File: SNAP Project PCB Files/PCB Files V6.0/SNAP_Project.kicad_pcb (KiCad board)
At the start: 4 copper layers, 66.7 x 47.2 mm, 108 parts, among them IC1 ADP121-AUJZ30R7, IC2 STM32WB35CCU7A, J1 USB_C_Receptacle_USB2.0, J3 Serial Wire Debug, J4 OLED Screen Conn, Q1 2N7000, Q2 2N7000, Q3 2N7000, Q4 SFH 310, Q5 2N7002KDW_R1_00001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

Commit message: Fix Button Issue
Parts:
- removed R29: 10k, Resistor_SMD:R_0805_2012Metric
- turned C30 to 0 degrees
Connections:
- SW5 pad 1: BUTT_2 -> GND
- SW5 pad 2: +3V0 -> BUTT_2
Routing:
- net GND: track 99.2 -> 90.2 mm, vias 344 -> 345
- net BUTT_2: track 0.86 -> 9.88 mm, vias 1 -> 0
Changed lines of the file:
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@@
   )
   (footprint "Capacitor_SMD:C_0402_1005Metric" (layer "F.Cu")
-    (at 106.37 89.8075 180)
+    (at 106.37 89.8075)
     (descr "Capacitor SMD 0402 (1005 Metric), square (rectangular) end terminal, IPC_7351 nominal, (Body size source: IPC-SM-782 page 76, https://www.pcb-3d.com/wordpress/wp-content/uploads/ipc-sm-782a_amendment_1_and_2.pdf), generated with kicad-footprint-generator")
     (tags "capacitor")
@@
     (fp_line (start 0.5 -0.25) (end 0.5 0.25) (layer "F.Fab") (width 0.1))
     (fp_line (start 0.5 0.25) (end -0.5 0.25) (layer "F.Fab") (width 0.1))
-    (pad "1" smd roundrect (at -0.48 0 180) (size 0.56 0.62) (layers "F.Cu" "F.Paste" "F.Mask") (roundrect_rratio 0.25)
+    (pad "1" smd roundrect (at -0.48 0) (size 0.56 0.62) (layers "F.Cu" "F.Paste" "F.Mask") (roundrect_rratio 0.25)
       (net 2 "GND") (pintype "passive"))
-    (pad "2" smd roundrect (at 0.48 0 180) (size 0.56 0.62) (layers "F.Cu" "F.Paste" "F.Mask") (roundrect_rratio 0.25)
+    (pad "2" smd roundrect (at 0.48 0) (size 0.56 0.62) (layers "F.Cu" "F.Paste" "F.Mask") (roundrect_rratio 0.25)
       (net 26 "BUTT_2") (pintype "passive"))
     (model "${KICAD6_3DMODEL_DIR}/Capacitor_SMD.3dshapes/C_0402_1005Metric.wrl"
@@
       (net 2 "GND") (pintype "passive"))
     (model "${KICAD6_3DMODEL_DIR}/Capacitor_SMD.3dshapes/C_0402_1005Metric.wrl"
-      (offset (xyz 0 0 0))
-      (scale (xyz 1 1 1))
-      (rotate (xyz 0 0 0))
-    )
-  )
-  (footprint "Resistor_SMD:R_0805_2012Metric" (layer "F.Cu")
-    (at 104.24 72.17)
-    (descr "Resistor SMD 0805 (2012 Metric), square (rectangular) end terminal, IPC_7351 nominal, (Body size source: IPC-SM-782 page 72, https://www.pcb-3d.com/wordpress/wp-content/uploads/ipc-sm-782a_amendment_1_and_2.pdf), generated with kicad-footprint-generator")
-    (tags "resistor")
-    (property "Sheetfile" "RF_MPU_OPAMP_PH.kicad_sch")
-    (property "Sheetname" "Amplification + Phototransistor + RF + MPU Circuit")
-    (attr smd)
-    (fp_text reference "R29" (at 0 -1.65) (layer "F.SilkS")
-      (effects (font (size 1 1) (thickness 0.15)))
-    )
-    (fp_text value "10k" (at 0 1.65) (layer "F.Fab")
-      (effects (font (size 1 1) (thickness 0.15)))
-    )
-    (fp_text user "${REFERENCE}" (at 0 0) (layer "F.Fab")
-      (effects (font (size 0.5 0.5) (thickness 0.08)))
-    )
-    (fp_line (start -0.227064 0.735) (end 0.227064 0.735) (layer "F.SilkS") (width 0.12))
-    (fp_line (start -0.227064 -0.735) (end 0.227064 -0.735) (layer "F.SilkS") (width 0.12))
-    (fp_line (start 1.68 -0.95) (end 1.68 0.95) (layer "F.CrtYd") (width 0.05))
-    (fp_line (start 1.68 0.95) (end -1.68 0.95) (layer "F.CrtYd") (width 0.05))
-    (fp_line (start -1.68 -0.95) (end 1.68 -0.95) (layer "F.CrtYd") (width 0.05))
-    (fp_line (start -1.68 0.95) (end -1.68 -0.95) (layer "F.CrtYd") (width 0.05))
-    (fp_line (start 1 0.625) (end -1 0.625) (layer "F.Fab") (width 0.1))
-    (fp_line (start -1 -0.625) (end 1 -0.625) (layer "F.Fab") (width 0.1))
-    (fp_line (start 1 -0.625) (end 1 0.625) (layer "F.Fab") (width 0.1))
-    (fp_line (start -1 0.625) (end -1 -0.625) (layer "F.Fab") (width 0.1))
-    (pad "1" smd roundrect (at -0.9125 0) (size 1.025 1.4) (layers "F.Cu" "F.Paste" "F.Mask") (roundrect_rratio 0.243902)
-      (net 26 "BUTT_2") (pintype "passive"))
-    (pad "2" smd roundrect (at 0.9125 0) (size 1.025 1.4) (layers "F.Cu" "F.Paste" "F.Mask") (roundrect_rratio 0.243902)
-      (net 2 "GND") (pintype "passive"))
-    (model "${KICAD6_3DMODEL_DIR}/Resistor_SMD.3dshapes/R_0805_2012Metric.wrl"
       (offset (xyz 0 0 0))
       (scale (xyz 1 1 1))
@@
     (fp_line (start -1.27 -2.92) (end -1.27 2.88) (layer "F.Fab") (width 0.1))
     (pad "1" thru_hole roundrect (at 0 0) (size 1.74 2.19) (drill 1.19) (layers *.Cu *.Mask) (roundrect_rratio 0.1436781609)
-      (net 26 "BUTT_2") (pinfunction "1") (pintype "passive"))
+      (net 2 "GND") (pinfunction "1") (pintype "passive"))
     (pad "2" thru_hole oval (at 2.54 0) (size 1.74 2.19) (drill 1.19) (layers *.Cu *.Mask)
-      (net 3 "+3V0") (pinfunction "2") (pintype "passive"))
+      (net 26 "BUTT_2") (pinfunction "2") (pintype "passive"))
     (model "${KICAD6_3DMODEL_DIR}/Connector_Molex.3dshapes/Molex_KK-254_AE-6410-02A_1x02_P2.54mm_Vertical.wrl"
       (offset (xyz 0 0 0))
@@
   (segment (start 113.88 95.12) (end 114.4 95.12) (width 0.25) (layer "F.Cu") (net 2))
   (segment (start 109.35 96.8075) (end 107.6 98.5575) (width 0.25) (layer "F.Cu") (net 2))
-  (segment (start 107.85 91.55) (end 107.85 95.1075) (width 0.25) (layer "F.Cu") (net 2))
   (segment (start 103.13 102.75) (end 103.44 103.06) (width 0.25) (layer "F.Cu") (net 2))
   (segment (start 99.125 111.075) (end 99.365773 111.315773) (width 0.25) (layer "F.Cu") (net 2))
@@
   (segment (start 75.94 109.7725) (end 75.34 110.3725) (width 1) (layer "F.Cu") (net 2))
   (segment (start 127.805 86.5425) (end 127.805 85.6175) (width 0.25) (layer "F.Cu") (net 2))
-  (segment (start 107.54 87.3675) (end 106.85 88.0575) (width 0.25) (layer "F.Cu") (net 2))
   (segment (start 118.3625 113.2975) (end 118.9975 113.2975) (width 0.5) (layer "F.Cu") (net 2))
   (segment (start 103.44 103.06) (end 103.44 102.54) (width 0.25) (layer "F.Cu") (net 2))
@@
   (segment (start 111.2 94.92) (end 111.2 94.58) (width 0.25) (layer "F.Cu") (net 2))
   (segment (start 106.47 107.28) (end 106.47 106.8575) (width 0.25) (layer "F.Cu") (net 2))
-  (segment (start 106.85 88.0575) (end 106.85 89.8075) (width 0.25) (layer "F.Cu") (net 2))
   (segment (start 103.2 103.3) (end 103.44 103.06) (width 0.25) (layer "F.Cu") (net 2))
   (segment (start 109.58 105.4875) (end 109.58 106.13) (width 0.25) (layer "F.Cu") (net 2))
@@
   (segment (start 119.83 113.3) (end 120.45 113.92) (width 0.5) (layer "F.Cu") (net 2))
   (segment (start 114.3175 92.8275) (end 114.325 92.82) (width 0.25) (layer "F.Cu") (net 2))
-  (segment (start 106.85 90.55) (end 107.85 91.55) (width 0.25) (layer "F.Cu") (net 2))
   (segment (start 111.525 118.145) (end 111.71 117.96) (width 0.25) (layer "F.Cu") (net 2))
   (segment (start 118.98 107.855) (end 118.98 108.355) (width 0.25) (layer "F.Cu") (net 2))
+  (segment (start 105.89 89.8075) (end 105.89 88.96) (width 0.25) (layer "F.Cu") (net 2))
   (segment (start 111.525 119.1) (end 111.525 118.145) (width 0.25) (layer "F.Cu") (net 2))
   (segment (start 88.875 108.4075) (end 88.875 110.25) (width 0.6) (layer "F.Cu") (net 2))
@@
   (segment (start 115.069273 116.125) (end 115.076773 116.1175) (width 0.25) (layer "F.Cu") (net 2))
   (segment (start 100.47 97.1075) (end 99.7875 97.1075) (width 0.25) (layer "F.Cu") (net 2))
-  (segment (start 106.85 89.8075) (end 106.85 90.55) (width 0.25) (layer "F.Cu") (net 2))
   (segment (start 113.875 116.125) (end 115.069273 116.125) (width 0.25) (layer "F.Cu") (net 2))
   (segment (start 86.65 92.425) (end 86.65 92.25) (width 0.25) (layer "F.Cu") (net 2))
@@
   (segment (start 110.625 112.35) (end 110.65 112.375) (width 0.25) (layer "F.Cu") (net 2))
   (segment (start 115.91 98.81) (end 115.925 98.825) (width 0.25) (layer "F.Cu") (net 2))
-  (segment (start 107.54 85.9275) (end 107.54 87.3675) (width 0.25) (layer "F.Cu") (net 2))
   (segment (start 105.35 92.5275) (end 105.35 91.675) (width 0.25) (layer "F.Cu") (net 2))
   (segment (start 128.0775 85.29) (end 128.055 85.2675) (width 0.25) (layer "F.Cu") (net 2))
   (segment (start 127.805 85.6175) (end 128.055 85.3675) (width 0.25) (layer "F.Cu") (net 2))
+  (segment (start 105.89 88.96) (end 105.9 88.95) (width 0.25) (layer "F.Cu") (net 2))
   (segment (start 94.75 97.8) (end 94.75 98.5775) (width 0.25) (layer "F.Cu") (net 2))
   (via (at 86.325 78.95) (size 0.55) (drill 0.25) (layers "F.Cu" "B.Cu") (net 2))
@@
   (via (at 123.26 115.93) (size 0.55) (drill 0.25) (layers "F.Cu" "B.Cu") (net 2))
   (via (at 101.25 120.52) (size 0.55) (drill 0.25) (layers "F.Cu" "B.Cu") (net 2))
+  (via (at 105.9 88.95) (size 0.55) (drill 0.25) (layers "F.Cu" "B.Cu") (net 2))
   (via (at 132.8 92.375) (size 0.55) (drill 0.25) (layers "F.Cu" "B.Cu") (net 2))
   (via (at 86.53 111.36) (size 0.55) (drill 0.25) (layers "F.Cu" "B.Cu") (net 2))
@@
   (segment (start 113.08 90.3775) (end 112.95 90.5075) (width 0.25) (layer "F.Cu") (net 25))
   (segment (start 113.84 85.9275) (end 113.84 87.9175) (width 0.25) (layer "F.Cu") (net 25))
-  (segment (start 105.89 89.8075) (end 105.89 88.96) (width 0.25) (layer "F.Cu") (net 26))
-  (segment (start 105.89 88.96) (end 105.9 88.95) (width 0.25) (layer "F.Cu") (net 26))
-  (via (at 105.9 88.95) (size 0.55) (drill 0.25) (layers "F.Cu" "B.Cu") (net 26))
+  (segment (start 107.85 91.55) (end 107.85 95.1075) (width 0.25) (layer "F.Cu") (net 26))
+  (segment (start 107.54 87.3675) (end 106.85 88.0575) (width 0.25) (layer "F.Cu") (net 26))
+  (segment (start 106.85 88.0575) (end 106.85 89.8075) (width 0.25) (layer "F.Cu") (net 26))
+  (segment (start 106.85 90.55) (end 107.85 91.55) (width 0.25) (layer "F.Cu") (net 26))
+  (segment (start 106.85 89.8075) (end 106.85 90.55) (width 0.25) (layer "F.Cu") (net 26))
+  (segment (start 107.54 85.9275) (end 107.54 87.3675) (width 0.25) (layer "F.Cu") (net 26))
   (segment (start 112 101.17) (end 112 101.770293) (width 0.2) (layer "F.Cu") (net 27))
   (segment (start 111.05 100.8075) (end 111.6375 100.8075) (width 0.2) (layer "F.Cu") (net 27))

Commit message: 4v Line fix
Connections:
- C2 pad 1: +3V0 -> +4V
- C3 pad 1: SW_ON -> +4V
- IC1 pad 5: +3V0 -> +4V
- L1 pad 1: SW_ON -> +4V
- U2 pad 5: SW_ON -> +4V
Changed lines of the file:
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@@
   (net 89 "Net-(C25-Pad1)")
   (net 90 "Net-(R18-Pad2)")
+  (net 91 "+4V")
   (footprint "Connector_Molex:Molex_KK-254_AE-6410-04A_1x04_P2.54mm_Vertical" (layer "F.Cu")
     (at 95.14 78.9275)
@@
       (net 20 "unconnected-(IC1-Pad4)") (pinfunction "NC") (pintype "no_connect"))
     (pad "5" smd rect locked (at 1.25 -0.95 180) (size 0.6 1.15) (layers "F.Cu" "F.Paste" "F.Mask")
-      (net 3 "+3V0") (pinfunction "VOUT") (pintype "passive"))
+      (net 91 "+4V") (pinfunction "VOUT") (pintype "passive"))
     (model "F:\\KiCad Libraries\\SamacSys_Parts.3dshapes\\ADP121-AUJZ33R7.stp"
       (offset (xyz 0 0 0))
@@
       (net 28 "MT3608_EN") (pinfunction "EN") (pintype "input"))
     (pad "5" smd roundrect (at 1.1375 0 270) (size 1.325 0.6) (layers "F.Cu" "F.Paste" "F.Mask") (roundrect_rratio 0.25)
-      (net 1 "SW_ON") (pinfunction "IN") (pintype "power_in"))
+      (net 91 "+4V") (pinfunction "IN") (pintype "power_in"))
     (pad "6" smd roundrect (at 1.1375 -0.95 270) (size 1.325 0.6) (layers "F.Cu" "F.Paste" "F.Mask") (roundrect_rratio 0.25)
       (net 67 "unconnected-(U2-Pad6)") (pinfunction "NC") (pintype "no_connect"))
@@
     (fp_line (start 1.6 -0.8) (end 1.6 0.8) (layer "F.Fab") (width 0.1))
     (pad "1" smd roundrect (at -1.475 0 180) (size 1.15 1.8) (layers "F.Cu" "F.Paste" "F.Mask") (roundrect_rratio 0.2173913043)
-      (net 3 "+3V0") (pintype "passive"))
+      (net 91 "+4V") (pintype "passive"))
     (pad "2" smd roundrect (at 1.475 0 180) (size 1.15 1.8) (layers "F.Cu" "F.Paste" "F.Mask") (roundrect_rratio 0.2173913043)
       (net 2 "GND") (pintype "passive"))
@@
     (fp_line (start 1.6 -0.8) (end 1.6 0.8) (layer "F.Fab") (width 0.1))
     (pad "1" smd roundrect (at -1.475 0 180) (size 1.15 1.8) (layers "F.Cu" "F.Paste" "F.Mask") (roundrect_rratio 0.2173913043)
-      (net 1 "SW_ON") (pintype "passive"))
+      (net 91 "+4V") (pintype "passive"))
     (pad "2" smd roundrect (at 1.475 0 180) (size 1.15 1.8) (layers "F.Cu" "F.Paste" "F.Mask") (roundrect_rratio 0.2173913043)
       (net 2 "GND") (pintype "passive"))
@@
     (fp_line (start -2.54 2.54) (end 2.54 2.54) (layer "F.Fab") (width 0.1))
     (pad "1" smd rect (at -2.4265 0) (size 1.903 2.79) (layers "F.Cu" "F.Paste" "F.Mask")
-      (net 1 "SW_ON") (pintype "passive"))
+      (net 91 "+4V") (pintype "passive"))
     (pad "2" smd rect (at 2.4265 0) (size 1.903 2.79) (layers "F.Cu" "F.Paste" "F.Mask")
       (net 15 "Net-(D1-Pad2)") (pintype "passive"))

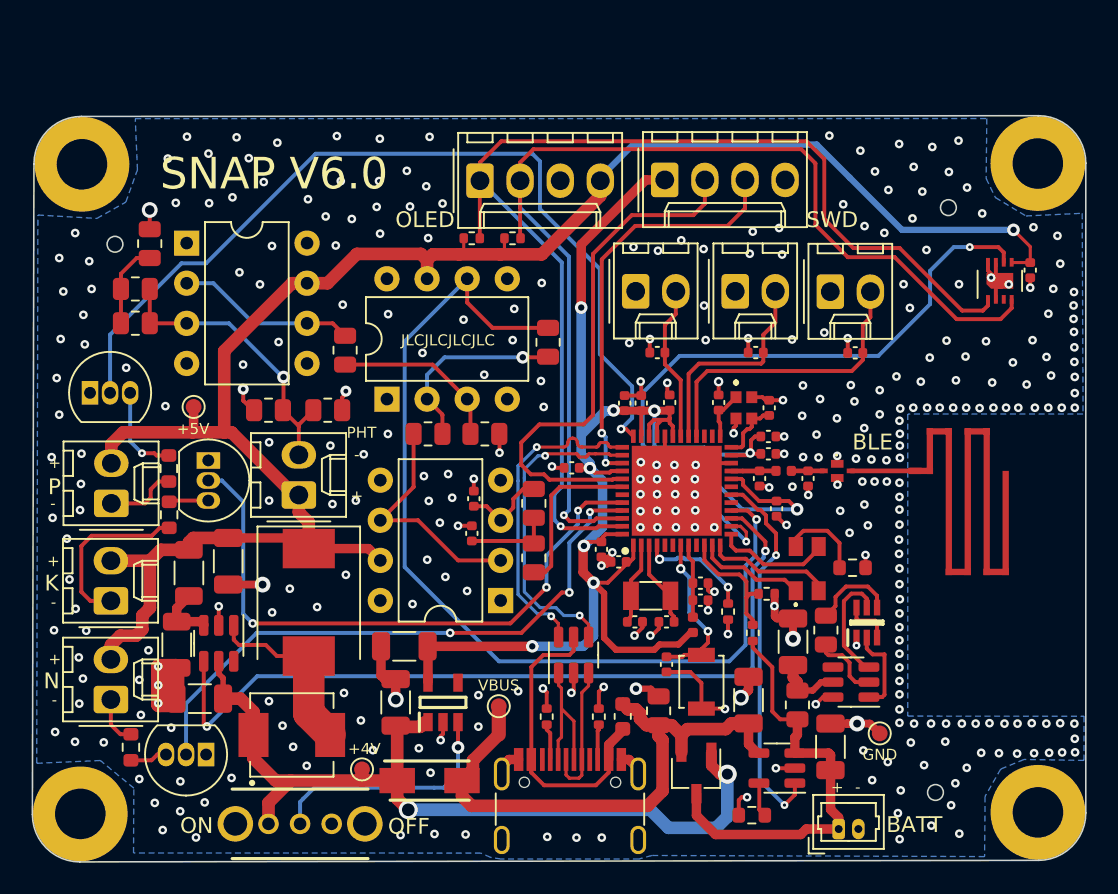
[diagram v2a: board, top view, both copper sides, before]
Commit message: USB Parity Fix
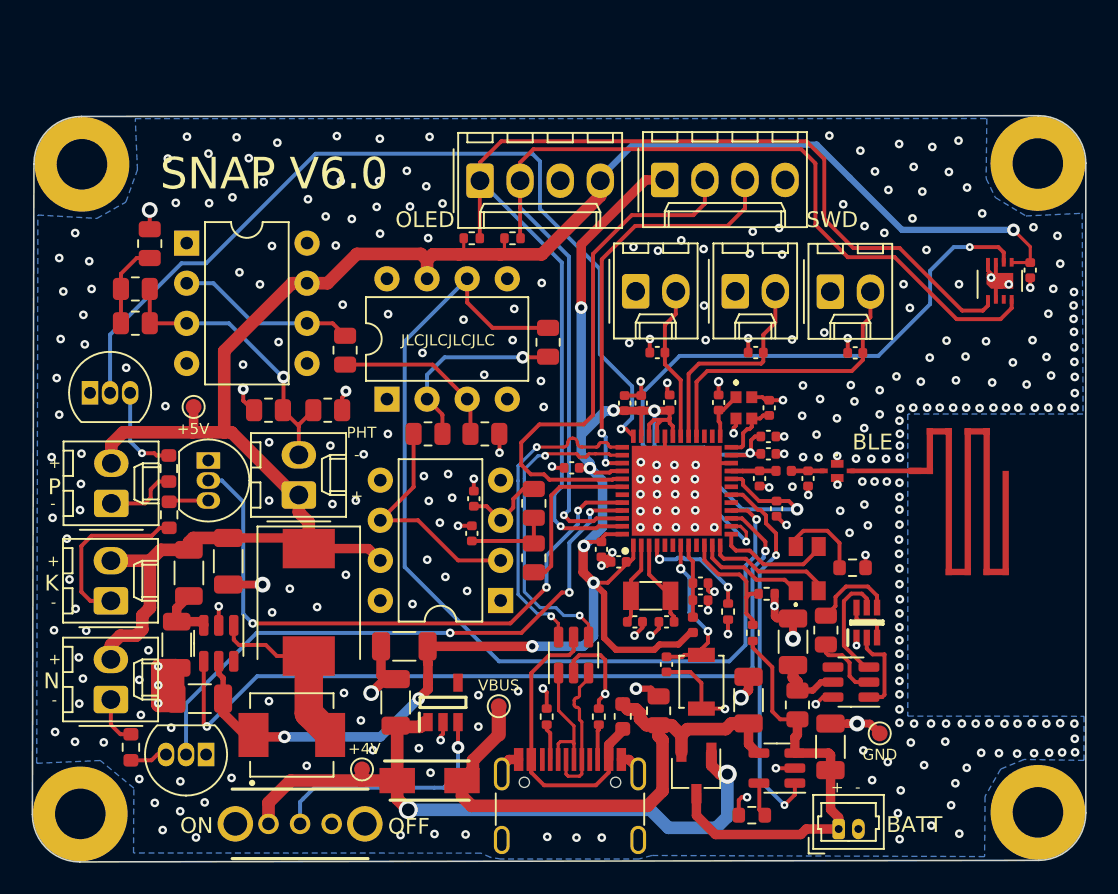
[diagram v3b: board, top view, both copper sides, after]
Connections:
- C2 pad 1: +4V -> +3V0
- C3 pad 1: +4V -> +3V0
- IC1 pad 5: +4V -> +3V0
- L1 pad 1: +4V -> +3V0
- U2 pad 5: +4V -> +3V0
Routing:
- net +3V0: track 104.3 -> 122.9 mm, vias 9 -> 11
- net SW_ON: track 55.0 -> 44.4 mm
- net GND: track 90.2 -> 94.3 mm, vias 345 -> 342
- net USB_CONN_D-: track 9.18 -> 7.98 mm
- added copper zone on In2.Cu, net GND
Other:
- outline, holes or cut-outs redrawn

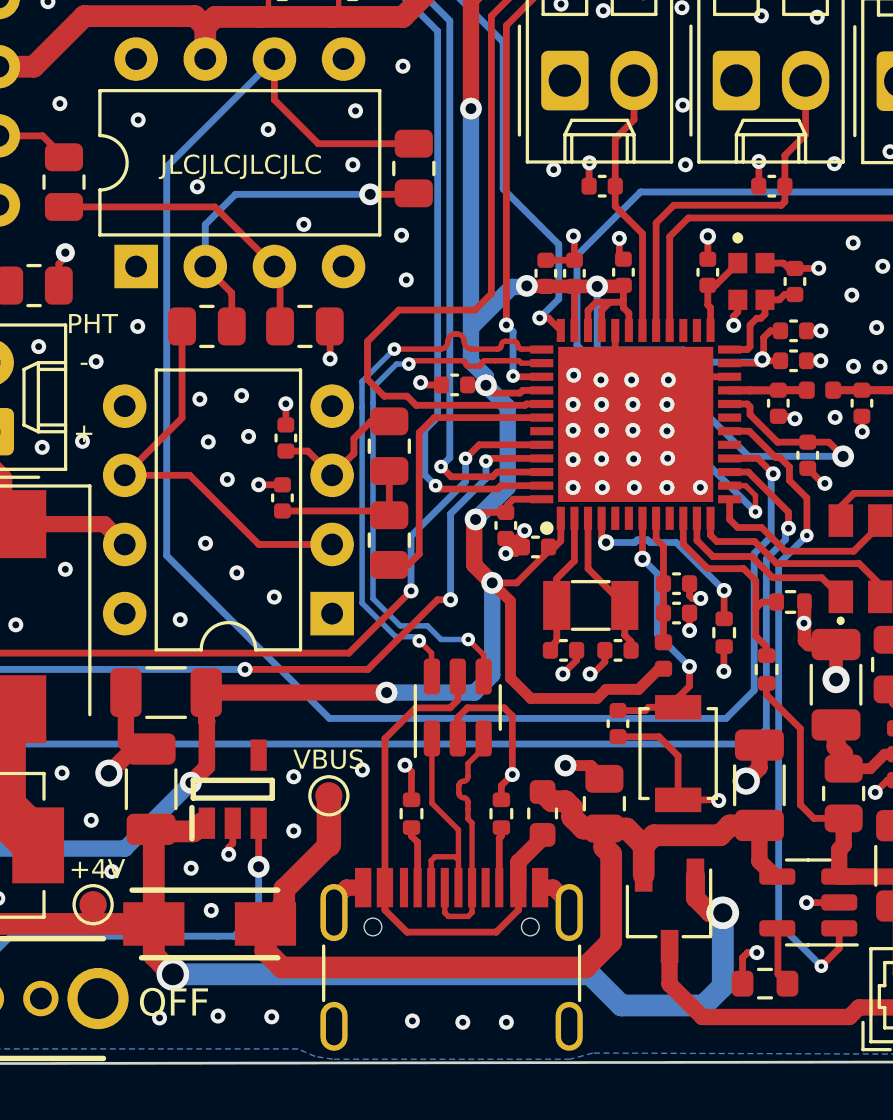
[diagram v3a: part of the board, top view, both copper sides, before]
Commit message: USB Fix 2 & 3V line fix
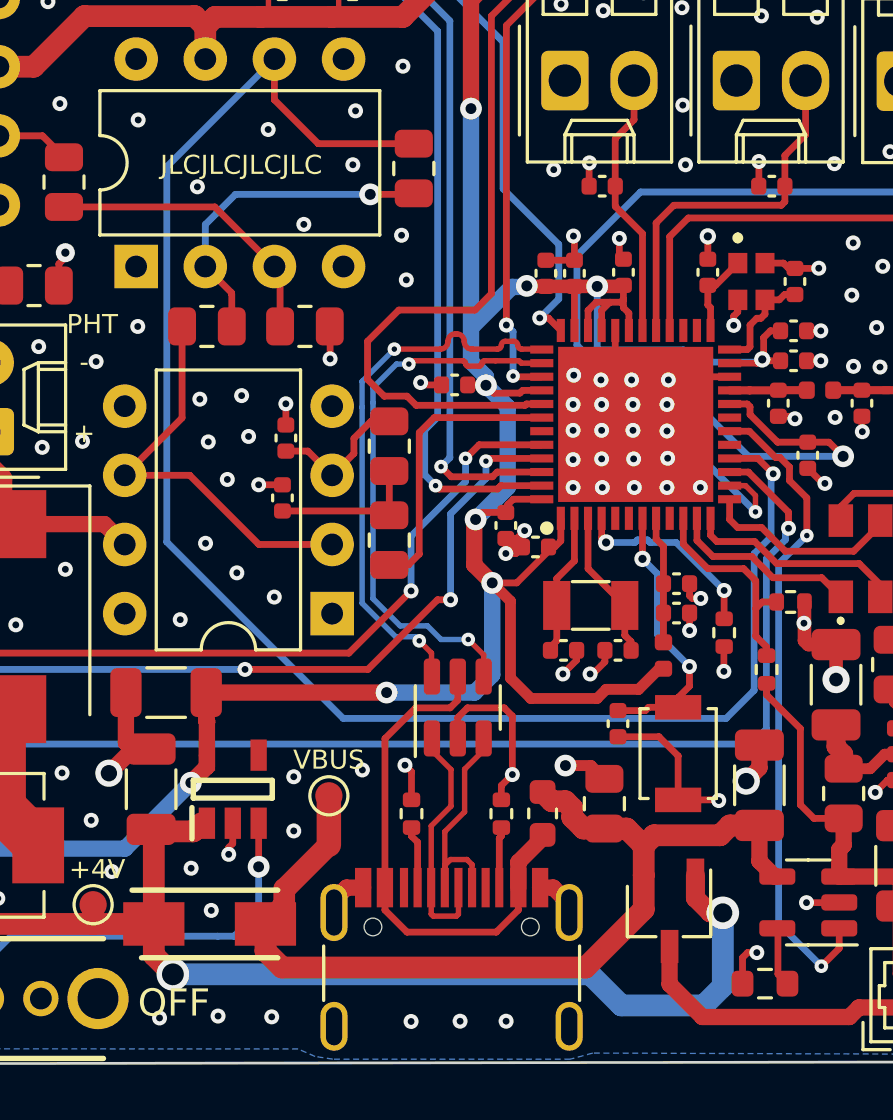
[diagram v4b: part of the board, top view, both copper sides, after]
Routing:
- net VBUS: track 36.8 -> 35.5 mm
- net USB_CONN_D-: track 7.98 -> 9.08 mm
- net USB_CONN_D+: track 9.09 -> 8.14 mm
